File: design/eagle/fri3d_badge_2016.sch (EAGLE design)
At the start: 43 parts, among them Q1 MOSFET-NCHANNEL2N7002PW, U1 MCP73831

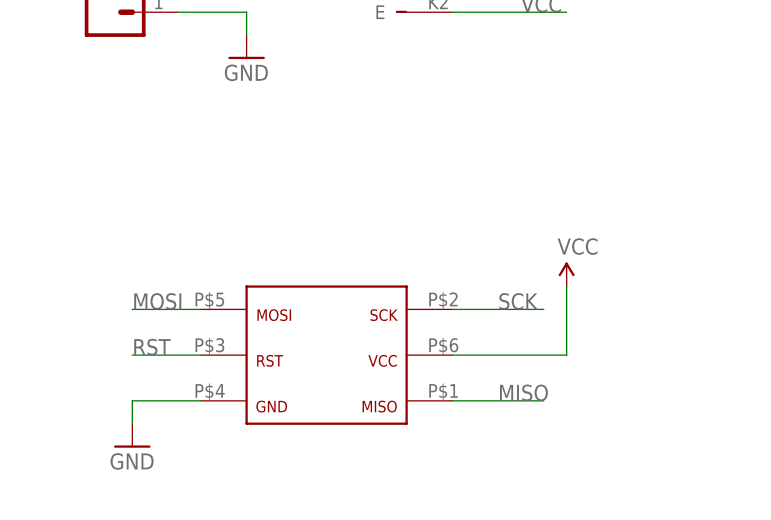
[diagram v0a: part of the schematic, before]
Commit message: redid Tag Connect mapping (same layout)
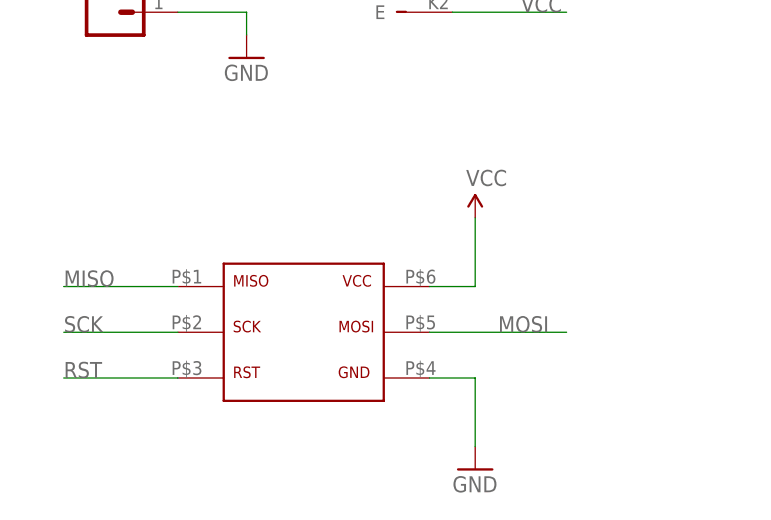
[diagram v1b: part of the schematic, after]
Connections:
- net GND: now also U$7.P$4; no longer U$7.P$6
- net MOSI: now also U$7.P$5; no longer U$7.P$4
- net RST: now also U$7.P$3; no longer U$7.P$5
- net SCK: now also U$7.P$2; no longer U$7.P$3
- net VCC: now also U$7.P$6; no longer U$7.P$2
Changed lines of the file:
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@@
 <instance part="U$5" gate="G$1" x="-25.4" y="137.16" rot="R180"/>
 <instance part="U$6" gate="G$1" x="-2.54" y="66.04"/>
-<instance part="U$7" gate="G$1" x="0" y="33.02" rot="R180"/>
-<instance part="GND11" gate="1" x="-27.94" y="15.24"/>
-<instance part="SUPPLY3" gate="G$1" x="20.32" y="33.02"/>
+<instance part="U$7" gate="G$1" x="-15.24" y="20.32"/>
+<instance part="GND11" gate="1" x="10.16" y="12.7"/>
+<instance part="SUPPLY3" gate="G$1" x="10.16" y="40.64"/>
 </instances>
 <busses>
@@
 </segment>
 <segment>
-<pinref part="U$7" gate="G$1" pin="P$6"/>
 <pinref part="GND11" gate="1" pin="GND"/>
-<wire x1="-20.32" y1="20.32" x2="-27.94" y2="20.32" width="0.1524" layer="91"/>
-<wire x1="-27.94" y1="20.32" x2="-27.94" y2="17.78" width="0.1524" layer="91"/>
+<pinref part="U$7" gate="G$1" pin="P$4"/>
+<wire x1="5.08" y1="22.86" x2="10.16" y2="22.86" width="0.1524" layer="91"/>
+<wire x1="10.16" y1="22.86" x2="10.16" y2="15.24" width="0.1524" layer="91"/>
 </segment>
 </net>
@@
 </segment>
 <segment>
-<pinref part="U$7" gate="G$1" pin="P$2"/>
+<pinref part="U$7" gate="G$1" pin="P$6"/>
 <pinref part="SUPPLY3" gate="G$1" pin="VCC"/>
-<wire x1="7.62" y1="25.4" x2="20.32" y2="25.4" width="0.1524" layer="91"/>
-<wire x1="20.32" y1="25.4" x2="20.32" y2="33.02" width="0.1524" layer="91"/>
+<wire x1="5.08" y1="33.02" x2="10.16" y2="33.02" width="0.1524" layer="91"/>
+<wire x1="10.16" y1="33.02" x2="10.16" y2="40.64" width="0.1524" layer="91"/>
 </segment>
 </net>
@@
 </segment>
 <segment>
-<pinref part="U$7" gate="G$1" pin="P$4"/>
-<wire x1="-20.32" y1="30.48" x2="-27.94" y2="30.48" width="0.1524" layer="91"/>
-<label x="-27.94" y="30.48" size="1.778" layer="95"/>
+<pinref part="U$7" gate="G$1" pin="P$5"/>
+<wire x1="5.08" y1="27.94" x2="20.32" y2="27.94" width="0.1524" layer="91"/>
+<label x="12.7" y="27.94" size="1.778" layer="95"/>
 </segment>
 </net>
@@
 </segment>
 <segment>
-<pinref part="U$7" gate="G$1" pin="P$5"/>
-<wire x1="-20.32" y1="25.4" x2="-27.94" y2="25.4" width="0.1524" layer="91"/>
-<label x="-27.94" y="25.4" size="1.778" layer="95"/>
+<pinref part="U$7" gate="G$1" pin="P$3"/>
+<wire x1="-22.86" y1="22.86" x2="-35.56" y2="22.86" width="0.1524" layer="91"/>
+<label x="-35.56" y="22.86" size="1.778" layer="95"/>
 </segment>
 </net>
@@
 </segment>
 <segment>
-<pinref part="U$7" gate="G$1" pin="P$3"/>
-<wire x1="7.62" y1="30.48" x2="17.78" y2="30.48" width="0.1524" layer="91"/>
-<label x="12.7" y="30.48" size="1.778" layer="95"/>
+<pinref part="U$7" gate="G$1" pin="P$2"/>
+<wire x1="-22.86" y1="27.94" x2="-35.56" y2="27.94" width="0.1524" layer="91"/>
+<label x="-35.56" y="27.94" size="1.778" layer="95"/>
 </segment>
 </net>
@@
 <segment>
 <pinref part="U$7" gate="G$1" pin="P$1"/>
-<wire x1="7.62" y1="20.32" x2="17.78" y2="20.32" width="0.1524" layer="91"/>
-<label x="12.7" y="20.32" size="1.778" layer="95"/>
-</segment>
-</net>
+<wire x1="-22.86" y1="33.02" x2="-35.56" y2="33.02" width="0.1524" layer="91"/>
+<label x="-35.56" y="33.02" size="1.778" layer="95"/>
+</segment>
+</net>

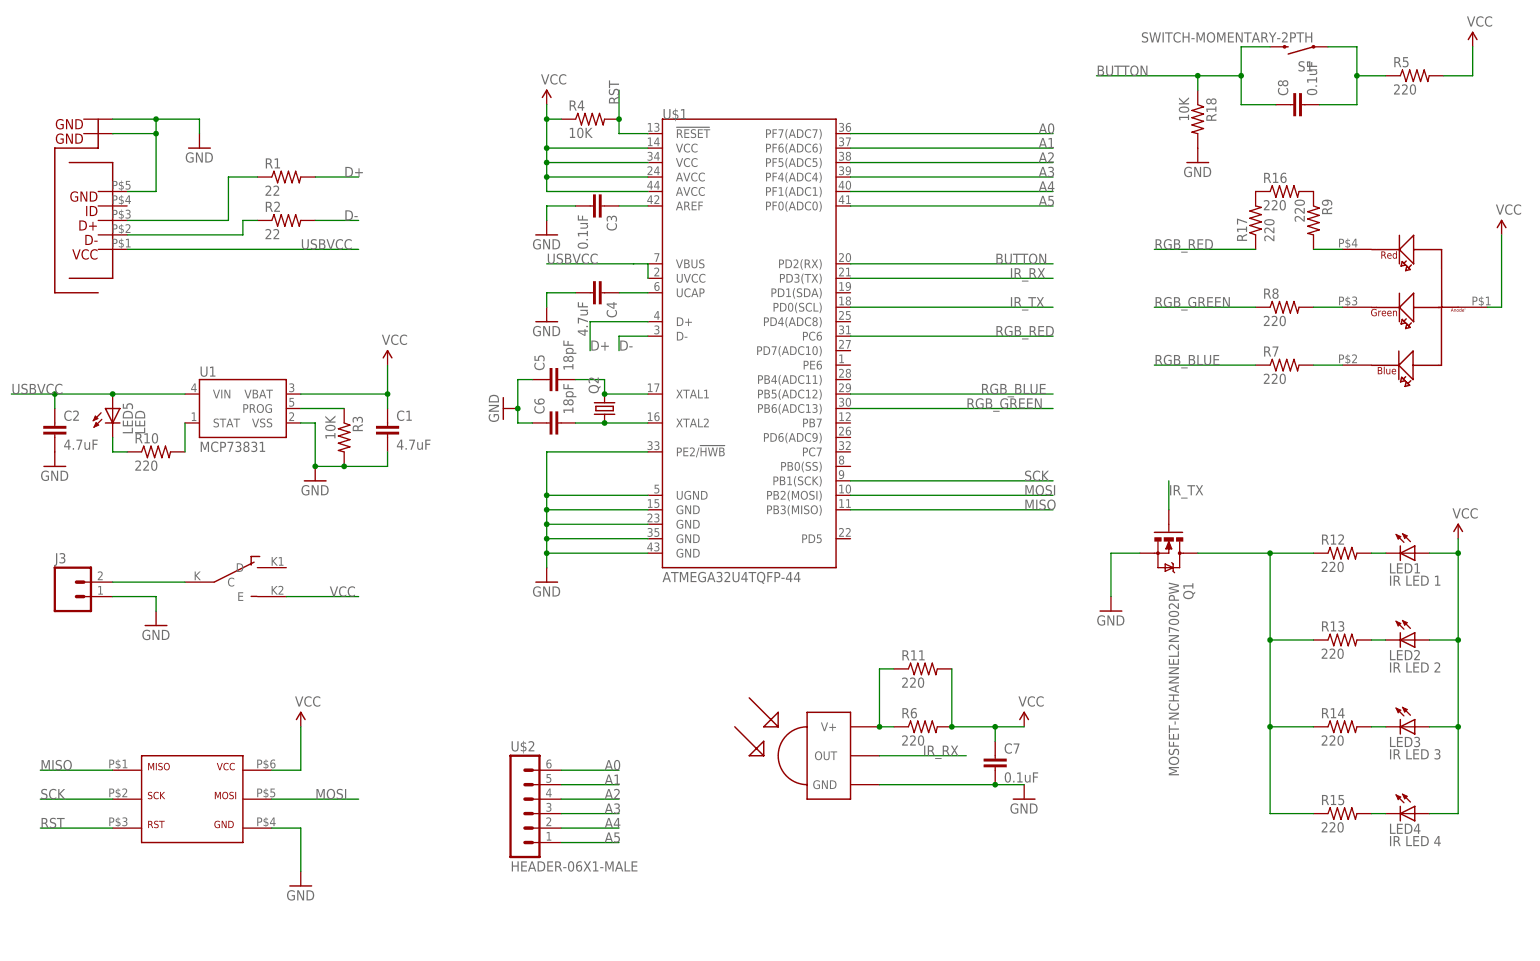
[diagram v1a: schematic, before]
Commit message: IR powered by pin, added headers, cleaned up silk
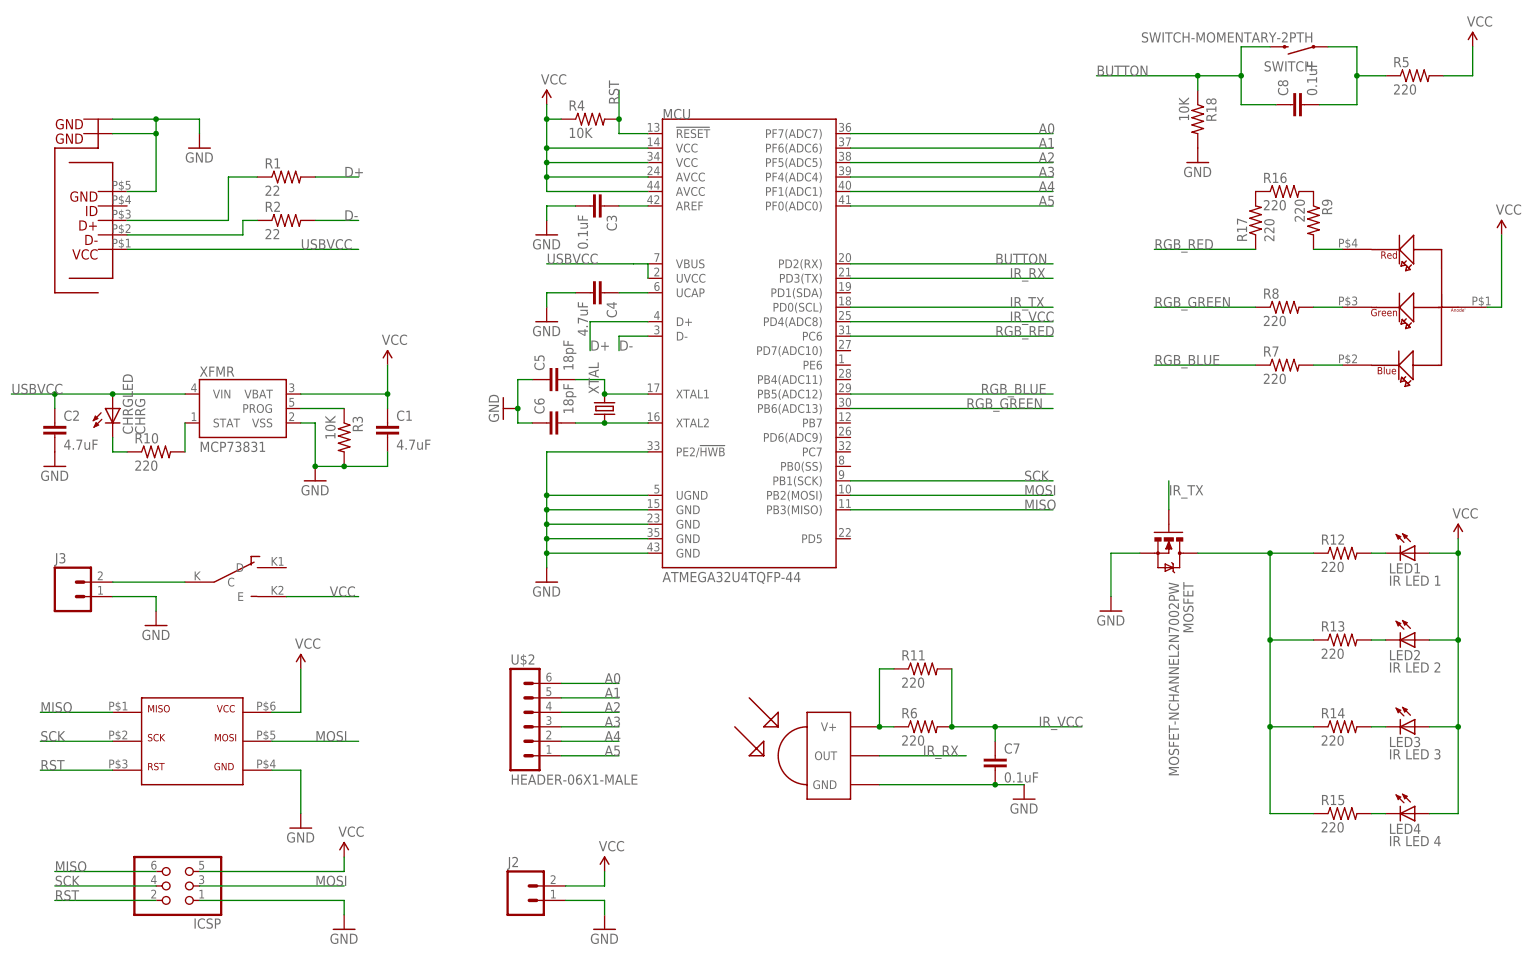
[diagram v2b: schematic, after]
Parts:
- added ICSP: (no value), SparkFun-Connectors:PINHD-2X3
- added J2: (no value), SparkFun-Connectors:M02PTH
- CHRGLED: value LED -> CHRG
- J3: device SparkFun-Connectors:M02JST-PTH-VERT -> SparkFun-Connectors:M02JST-PTH-2
- renumbered LED5 to CHRGLED, Q1 to MOSFET, Q2 to XTAL, S1 to SWITCH, U$1 to MCU, U1 to XFMR
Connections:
- new net IR_VCC: C7.1, MCU.PD4(ADC8), R11.2, R6.2
- net GND: now also ICSP.1, J2.1
- net MISO: now also ICSP.6
- net MOSI: now also ICSP.3
- net RST: now also ICSP.2
- net SCK: now also ICSP.4
- net VCC: now also ICSP.5, J2.2; no longer C7.1, R11.2, R6.2
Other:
- moved on the sheet: U$2

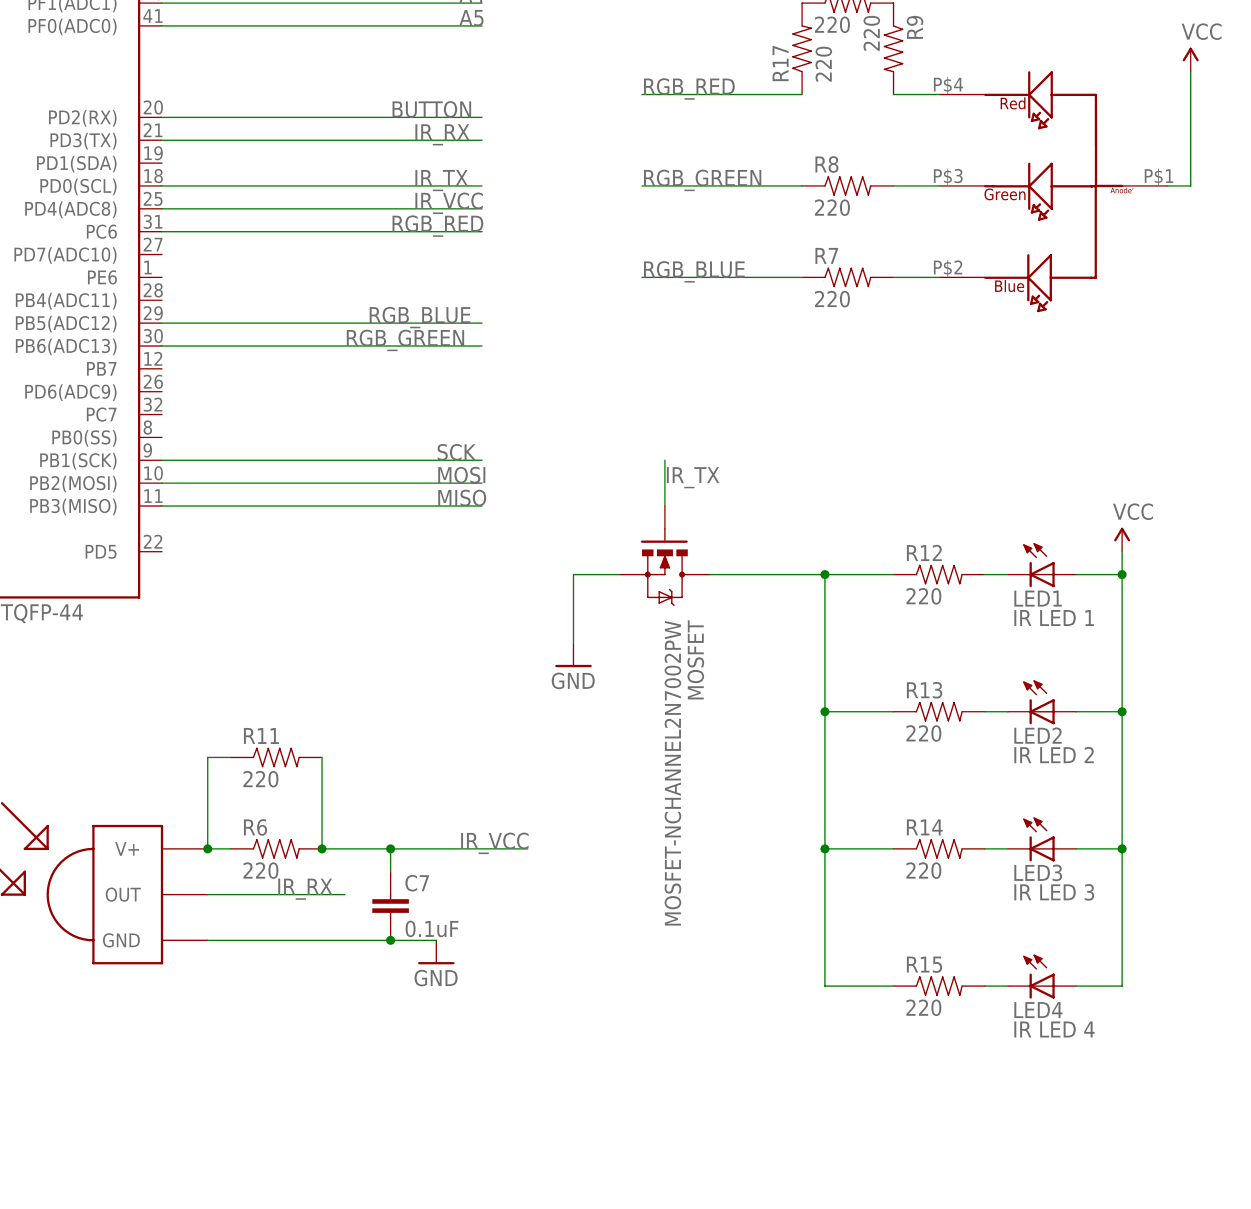
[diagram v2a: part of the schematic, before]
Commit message: attached IR/MOSFET to correct pin for IRremote
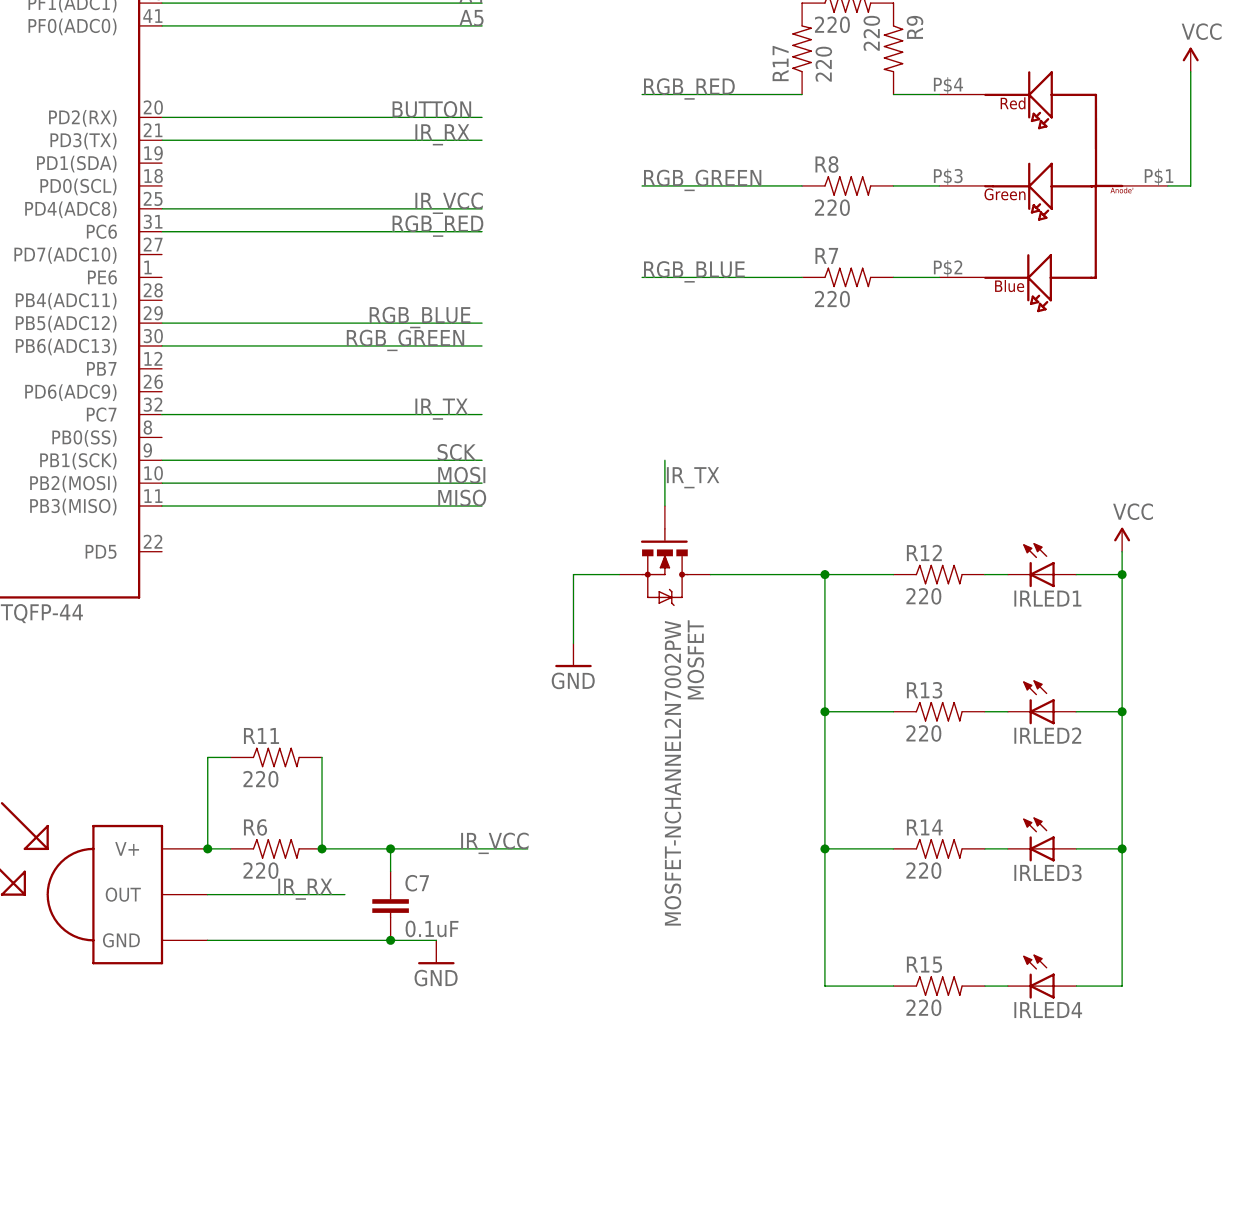
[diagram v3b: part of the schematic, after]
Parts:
- IRLED1: value IR LED 1 -> (none)
- IRLED2: value IR LED 2 -> (none)
- IRLED3: value IR LED 3 -> (none)
- IRLED4: value IR LED 4 -> (none)
- renumbered LED1 to IRLED1, LED2 to IRLED2, LED3 to IRLED3, LED4 to IRLED4
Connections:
- net IR_TX: now also MCU.PC7; no longer MCU.PD0(SCL)
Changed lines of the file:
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@@
 <attributes>
 <attribute name="CNAME" value="Fri3d Camp Badge"/>
-<attribute name="CREVISION" value="0"/>
+<attribute name="CREVISION" value="4"/>
 <attribute name="DESIGNER" value="Christophe VG"/>
 </attributes>
@@
 <part name="R16" library="SparkFun-Passives" deviceset="RESISTOR" device="0805-RES" value="220"/>
 <part name="R17" library="SparkFun-Passives" deviceset="RESISTOR" device="0805-RES" value="220"/>
-<part name="LED1" library="led" deviceset="LED" device="CHIPLED_0805" value="IR LED 1"/>
-<part name="LED2" library="led" deviceset="LED" device="CHIPLED_0805" value="IR LED 2"/>
-<part name="LED3" library="led" deviceset="LED" device="CHIPLED_0805" value="IR LED 3"/>
-<part name="LED4" library="led" deviceset="LED" device="CHIPLED_0805" value="IR LED 4"/>
+<part name="IRLED1" library="led" deviceset="LED" device="CHIPLED_0805"/>
+<part name="IRLED2" library="led" deviceset="LED" device="CHIPLED_0805"/>
+<part name="IRLED3" library="led" deviceset="LED" device="CHIPLED_0805"/>
+<part name="IRLED4" library="led" deviceset="LED" device="CHIPLED_0805"/>
 <part name="XTAL" library="crystal" deviceset="CRYSTAL" device="HC49S"/>
 <part name="J3" library="SparkFun-Connectors" deviceset="M02" device="JST-PTH-2"/>
@@
 <instance part="R16" gate="G$1" x="182.88" y="134.62"/>
 <instance part="R17" gate="G$1" x="177.8" y="129.54" rot="R90"/>
-<instance part="LED1" gate="G$1" x="205.74" y="71.12" rot="R270"/>
-<instance part="LED2" gate="G$1" x="205.74" y="55.88" rot="R270"/>
-<instance part="LED3" gate="G$1" x="205.74" y="40.64" rot="R270"/>
-<instance part="LED4" gate="G$1" x="205.74" y="25.4" rot="R270"/>
+<instance part="IRLED1" gate="G$1" x="205.74" y="71.12" rot="R270"/>
+<instance part="IRLED2" gate="G$1" x="205.74" y="55.88" rot="R270"/>
+<instance part="IRLED3" gate="G$1" x="205.74" y="40.64" rot="R270"/>
+<instance part="IRLED4" gate="G$1" x="205.74" y="25.4" rot="R270"/>
 <instance part="XTAL" gate="G$1" x="63.5" y="96.52" rot="R90"/>
 <instance part="J3" gate="G$1" x="-30.48" y="63.5"/>
@@
 <pinref part="SUPPLY4" gate="G$1" pin="VCC"/>
 <wire x1="213.36" y1="25.4" x2="213.36" y2="40.64" width="0.1524" layer="91"/>
-<pinref part="LED4" gate="G$1" pin="A"/>
+<pinref part="IRLED4" gate="G$1" pin="A"/>
 <wire x1="213.36" y1="40.64" x2="213.36" y2="55.88" width="0.1524" layer="91"/>
 <wire x1="213.36" y1="55.88" x2="213.36" y2="71.12" width="0.1524" layer="91"/>
 <wire x1="213.36" y1="71.12" x2="213.36" y2="73.66" width="0.1524" layer="91"/>
 <wire x1="208.28" y1="25.4" x2="213.36" y2="25.4" width="0.1524" layer="91"/>
-<pinref part="LED3" gate="G$1" pin="A"/>
+<pinref part="IRLED3" gate="G$1" pin="A"/>
 <wire x1="208.28" y1="40.64" x2="213.36" y2="40.64" width="0.1524" layer="91"/>
 <junction x="213.36" y="40.64"/>
-<pinref part="LED2" gate="G$1" pin="A"/>
+<pinref part="IRLED2" gate="G$1" pin="A"/>
 <wire x1="208.28" y1="55.88" x2="213.36" y2="55.88" width="0.1524" layer="91"/>
 <junction x="213.36" y="55.88"/>
-<pinref part="LED1" gate="G$1" pin="A"/>
+<pinref part="IRLED1" gate="G$1" pin="A"/>
 <wire x1="208.28" y1="71.12" x2="213.36" y2="71.12" width="0.1524" layer="91"/>
 <junction x="213.36" y="71.12"/>
@@
 </segment>
 <segment>
-<pinref part="MCU" gate="G$1" pin="PD0(SCL)"/>
-<wire x1="106.68" y1="114.3" x2="142.24" y2="114.3" width="0.1524" layer="91"/>
-<label x="134.62" y="114.3" size="1.778" layer="95"/>
+<pinref part="MCU" gate="G$1" pin="PC7"/>
+<wire x1="106.68" y1="88.9" x2="142.24" y2="88.9" width="0.1524" layer="91"/>
+<label x="134.62" y="88.9" size="1.778" layer="95"/>
 </segment>
 </net>
@@
 <segment>
 <pinref part="R12" gate="G$1" pin="2"/>
-<pinref part="LED1" gate="G$1" pin="C"/>
+<pinref part="IRLED1" gate="G$1" pin="C"/>
 <wire x1="200.66" y1="71.12" x2="198.12" y2="71.12" width="0.1524" layer="91"/>
 </segment>
@@
 <segment>
 <pinref part="R13" gate="G$1" pin="2"/>
-<pinref part="LED2" gate="G$1" pin="C"/>
+<pinref part="IRLED2" gate="G$1" pin="C"/>
 <wire x1="200.66" y1="55.88" x2="198.12" y2="55.88" width="0.1524" layer="91"/>
 </segment>
@@
 <segment>
 <pinref part="R14" gate="G$1" pin="2"/>
-<pinref part="LED3" gate="G$1" pin="C"/>
+<pinref part="IRLED3" gate="G$1" pin="C"/>
 <wire x1="200.66" y1="40.64" x2="198.12" y2="40.64" width="0.1524" layer="91"/>
 </segment>
@@
 <segment>
 <pinref part="R15" gate="G$1" pin="2"/>
-<pinref part="LED4" gate="G$1" pin="C"/>
+<pinref part="IRLED4" gate="G$1" pin="C"/>
 <wire x1="200.66" y1="25.4" x2="198.12" y2="25.4" width="0.1524" layer="91"/>
 </segment>
